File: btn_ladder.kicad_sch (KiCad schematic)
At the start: 14 parts, among them SW3 TS24CA, SW4 TS24CA, SW5 TS24CA, SW6 TS24CA, SW7 TS24CA, SW8 TS24CA

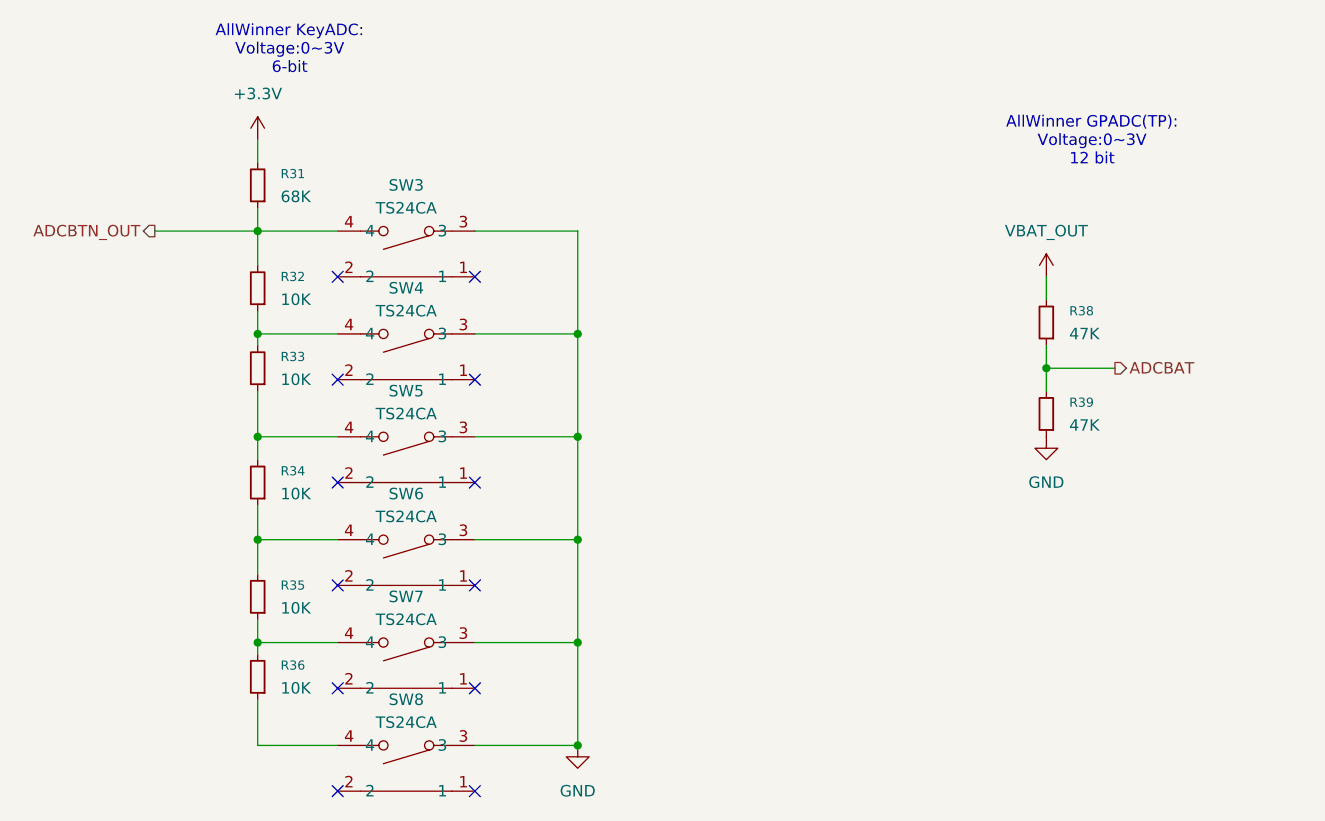
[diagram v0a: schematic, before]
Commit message: V0.3.1 bugfix
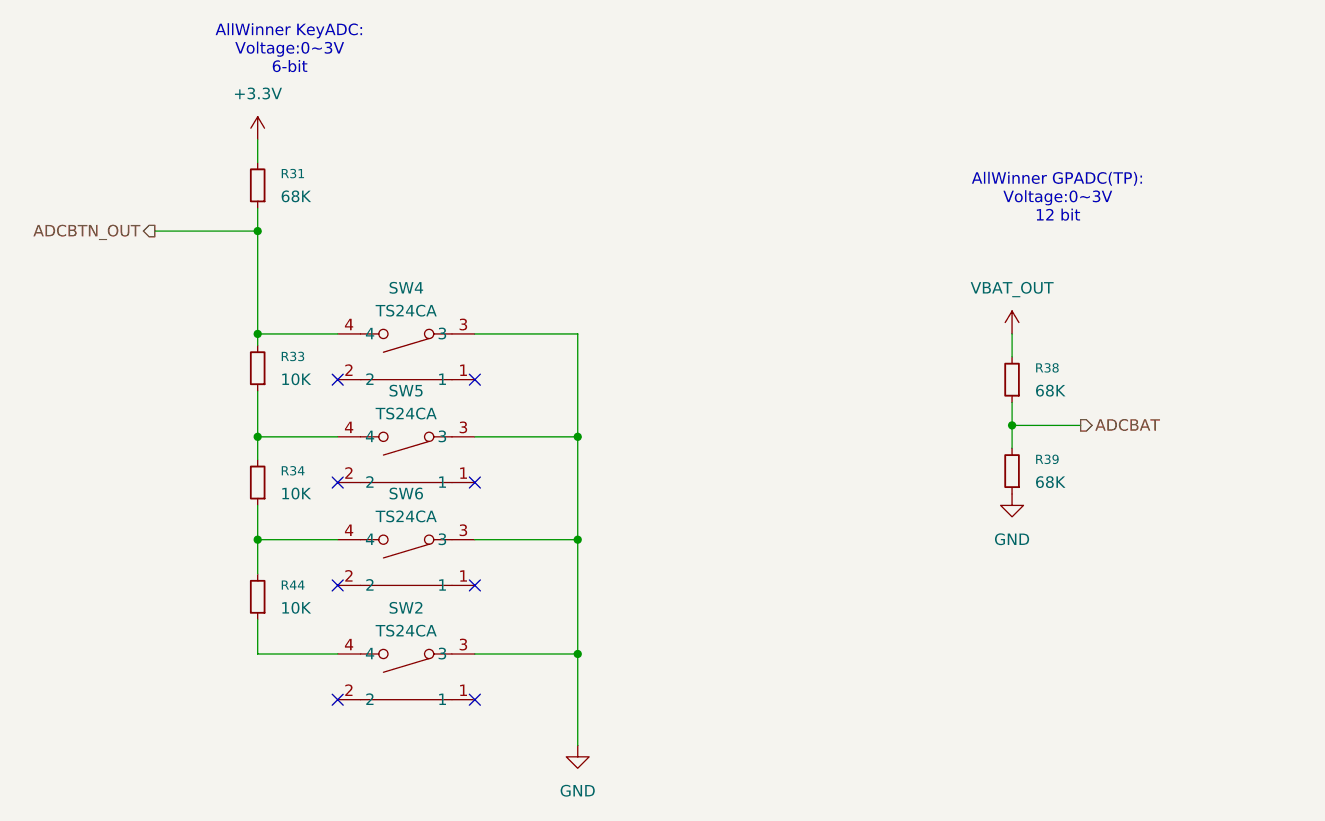
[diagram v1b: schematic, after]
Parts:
- removed R32, R35, R36: 10K, Resistor_SMD:R_0603_1608Metric, symbol Device:R_Small
- removed SW3, SW7, SW8: TS24CA, EasyEDA:SW-SMD_TS24CA, symbol EasyEDA_old:TS24CA
- added R44: 10K, Resistor_SMD:R_0603_1608Metric, symbol Device:R_Small
- added SW2: TS24CA, EasyEDA:SW-SMD_TS24CA, symbol EasyEDA_old:TS24CA
- R38, R39: value 47K -> 68K
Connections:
- net ADCBTN_OUT: now also R33.2, SW4.4
- net GND: now also SW2.3
- net at R34.1, SW6.4: now also R44.2
- new net: R44.1, SW2.4
- no-connect marks 12 -> 8
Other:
- moved on the sheet: R38, R39

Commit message: V0.5
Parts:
- added C46: 100nF, Capacitor_SMD:C_0603_1608Metric, symbol Device:C_Small
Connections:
- net ADCBAT: now also C46.1
- net GND: now also SW2.1, SW2.2, SW4.1, SW4.2, SW5.1, SW5.2, SW6.1, SW6.2, C46.2
- no-connect marks 8 -> 0
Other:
- note added: "ADC记得加电容哦 否则可能采样波动大 感谢和光老师"
